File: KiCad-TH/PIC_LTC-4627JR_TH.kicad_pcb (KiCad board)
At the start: 2 copper layers, 0 parts

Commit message: PCB Routing Round 5 Begins
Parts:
- added J1: Conn_01x05_Male, Pin_Headers:Pin_Header_Straight_1x05_Pitch2.54mm, F.Cu at (95.9, 113.7)
- added J2: Conn_01x04, Connectors_JST:JST_PH_B4B-PH-K_04x2.00mm_Straight, F.Cu at (104.1, 119.4)
- added L1: LTC-4627JR, LTC-4627JR:LTC-4627JR, F.Cu at (114.5, 83.8)
- added Q1: Q_NPN_EBC, TO_SOT_Packages_THT:TO-92_Inline_Narrow_Oval, F.Cu at (119.4, 95.2)
- added Q2: Q_NPN_EBC, TO_SOT_Packages_THT:TO-92_Inline_Narrow_Oval, F.Cu at (100.3, 95.2)
- added Q3: Q_NPN_EBC, TO_SOT_Packages_THT:TO-92_Inline_Narrow_Oval, F.Cu at (125.7, 95.2)
- added Q4: Q_NPN_EBC, TO_SOT_Packages_THT:TO-92_Inline_Narrow_Oval, F.Cu at (113.0, 95.2)
- added Q5: Q_NPN_EBC, TO_SOT_Packages_THT:TO-92_Inline_Narrow_Oval, F.Cu at (106.7, 95.2)
- added R1: 120, Resistors_THT:R_Axial_DIN0207_L6.3mm_D2.5mm_P10.16mm_Horizontal, F.Cu at (98.4, 99.1)
- added R10: 1k, Resistors_THT:R_Axial_DIN0207_L6.3mm_D2.5mm_P10.16mm_Horizontal, F.Cu at (114.3, 99.1)
- added R11: 1k, Resistors_THT:R_Axial_DIN0207_L6.3mm_D2.5mm_P10.16mm_Horizontal, F.Cu at (130.2, 99.1)
- added R12: 1k, Resistors_THT:R_Axial_DIN0207_L6.3mm_D2.5mm_P10.16mm_Horizontal, F.Cu at (104.8, 99.1)
- added R13: 1k, Resistors_THT:R_Axial_DIN0207_L6.3mm_D2.5mm_P10.16mm_Horizontal, F.Cu at (123.8, 99.1)
- added R2: 120, Resistors_THT:R_Axial_DIN0207_L6.3mm_D2.5mm_P10.16mm_Horizontal, F.Cu at (133.3, 99.1)
- added R3: 120, Resistors_THT:R_Axial_DIN0207_L6.3mm_D2.5mm_P10.16mm_Horizontal, F.Cu at (120.7, 99.1)
- added R4: 120, Resistors_THT:R_Axial_DIN0207_L6.3mm_D2.5mm_P10.16mm_Horizontal, F.Cu at (111.1, 99.1)
- added R5: 120, Resistors_THT:R_Axial_DIN0207_L6.3mm_D2.5mm_P10.16mm_Horizontal, F.Cu at (117.5, 99.1)
- added R6: 120, Resistors_THT:R_Axial_DIN0207_L6.3mm_D2.5mm_P10.16mm_Horizontal, F.Cu at (95.2, 99.1)
- added R7: 120, Resistors_THT:R_Axial_DIN0207_L6.3mm_D2.5mm_P10.16mm_Horizontal, F.Cu at (101.6, 99.1)
- added R8: 120, Resistors_THT:R_Axial_DIN0207_L6.3mm_D2.5mm_P10.16mm_Horizontal, F.Cu at (127.0, 99.1)
- added R9: 1k, Resistors_THT:R_Axial_DIN0207_L6.3mm_D2.5mm_P10.16mm_Horizontal, F.Cu at (108.0, 99.1)
- added U1: PIC16F18344-P, Housings_DIP:DIP-20_W7.62mm, F.Cu at (109.9, 121.3)

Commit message: PCB #5 Looking Good Still Needs Polish
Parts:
- moved R11 29.2 mm to (101.0, 99.1)
- moved Q3 27.3 mm to (98.4, 95.2)
- moved R9 25.4 mm to (133.3, 99.1)
- moved Q5 24.1 mm to (130.8, 95.2)
- moved R1 21.6 mm to (120.0, 99.1)
- moved R10 15.9 mm to (130.2, 99.1)
- moved J1 14.0 mm to (95.9, 99.7), turned to 0 degrees
- moved R7 12.1 mm to (113.7, 99.1)
- moved Q4 12.1 mm to (125.1, 95.2)
- moved R6 10.8 mm to (106.0, 99.1)
- moved R2 10.8 mm to (122.6, 99.1)
- moved R5 8.89 mm to (108.6, 99.1)
- moved R13 6.35 mm to (117.5, 99.1)
- moved Q2 4.45 mm to (104.8, 95.2)
- moved R3 4.44 mm to (125.1, 99.1)
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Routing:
- net /VPP: track 0.00 -> 40.8 mm, vias 0 -> 4
- net /DIG_2: track 0.00 -> 38.1 mm, vias 0 -> 2
- net /I2CCL: track 0.00 -> 36.5 mm, vias 0 -> 1
- net /DIG_4: track 0.00 -> 34.9 mm, vias 0 -> 2
- net Net-(L1-Pad15): track 0.00 -> 33.4 mm, vias 0 -> 3
- net /I2CDA: track 0.00 -> 32.2 mm, vias 0 -> 1
- net Net-(L1-Pad5): track 0.00 -> 30.4 mm, vias 0 -> 2
- net /ICSPCLK: track 0.00 -> 28.2 mm, vias 0 -> 2
- net /DIG_L: track 0.00 -> 24.8 mm, vias 0 -> 2
- net Net-(L1-Pad13): track 0.00 -> 24.5 mm, vias 0 -> 2
- net Net-(R5-Pad2): track 0.00 -> 24.1 mm, vias 0 -> 2
- net Net-(R7-Pad2): track 0.00 -> 24.1 mm, vias 0 -> 2
- net Net-(R6-Pad2): track 0.00 -> 24.1 mm, vias 0 -> 2
- net Net-(R4-Pad2): track 0.00 -> 24.1 mm, vias 0 -> 2
- net Net-(L1-Pad16): track 0.00 -> 22.7 mm
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- added copper zone on F.Cu, net GND
- added copper zone on B.Cu, net VCC
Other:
- net class Default: trace_width 0.1524 -> 0.25

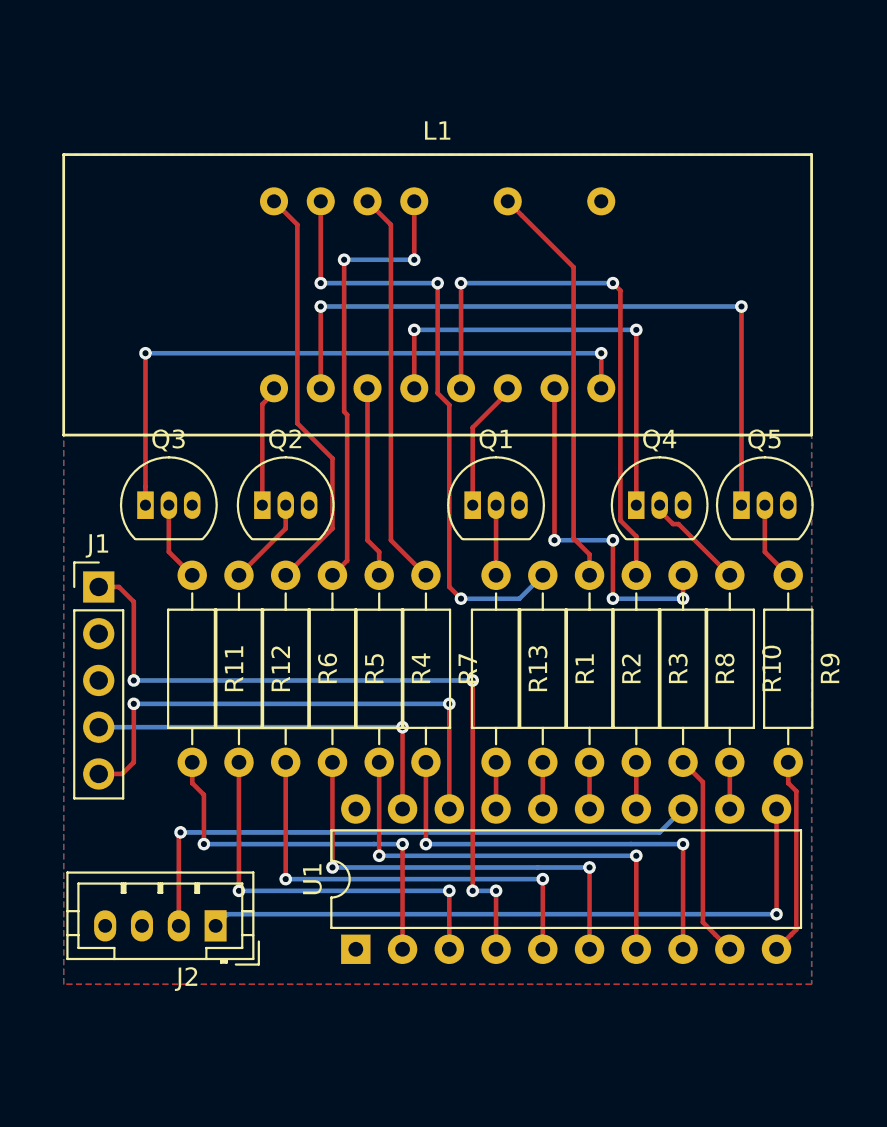
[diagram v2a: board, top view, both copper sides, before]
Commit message: PCB#5 now with Vpp pull-up resistor
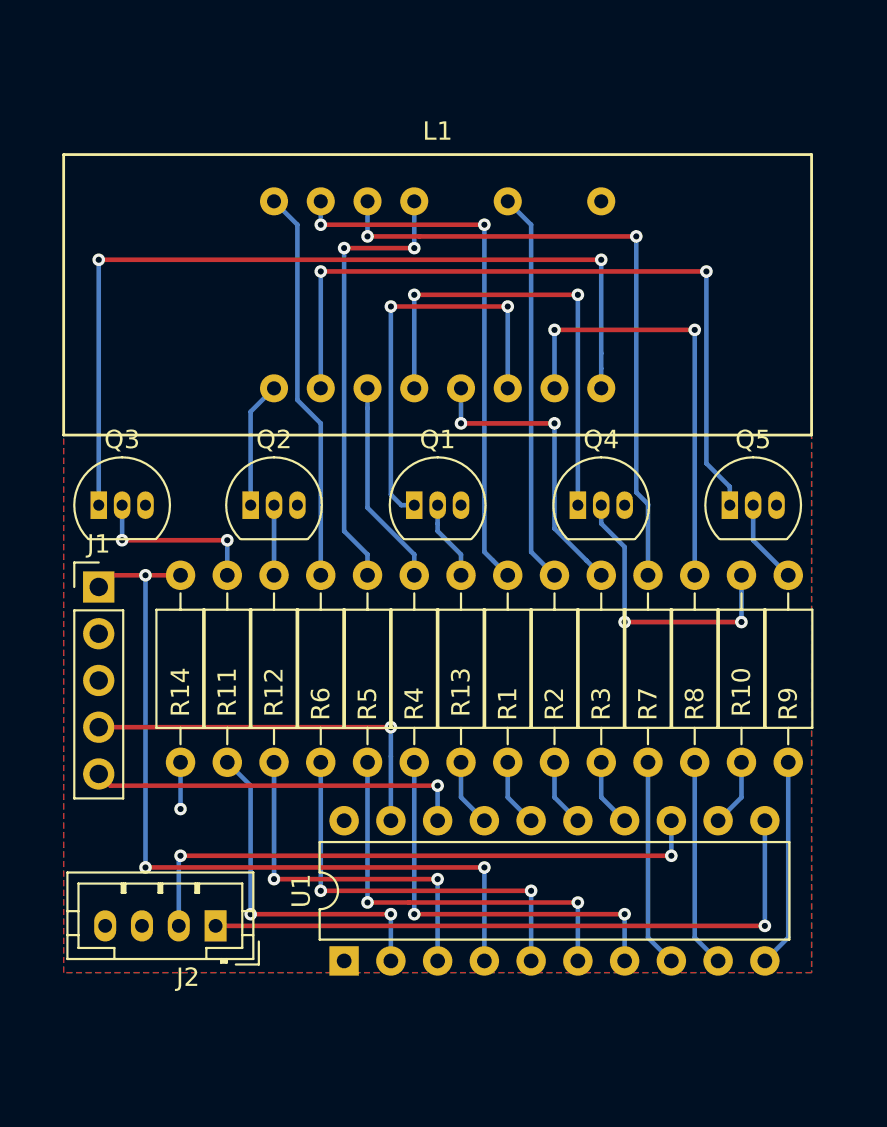
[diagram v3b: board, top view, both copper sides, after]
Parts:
- added R14: 10k, Resistors_THT:R_Axial_DIN0207_L6.3mm_D2.5mm_P10.16mm_Horizontal, F.Cu at (100.3, 99.1)
- moved R7 12.1 mm to (125.7, 99.1)
- moved Q1 3.17 mm to (113.0, 95.2)
- moved Q4 3.17 mm to (121.9, 95.2)
- moved Q3 2.54 mm to (95.9, 95.2)
- moved R1 1.91 mm to (118.1, 99.1)
- moved R11 1.91 mm to (102.9, 99.1)
- moved R12 1.91 mm to (105.4, 99.1)
- moved R13 1.91 mm to (115.6, 99.1)
- moved R2 1.91 mm to (120.7, 99.1)
- moved R3 1.91 mm to (123.2, 99.1)
- moved R4 1.91 mm to (113.0, 99.1)
- moved R5 1.91 mm to (110.5, 99.1)
- moved R6 1.91 mm to (108.0, 99.1)
- moved U1 0.90 mm to (109.2, 120.0)
- moved Q2 0.64 mm to (104.1, 95.2)
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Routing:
- net /DIG_3: track 7.23 -> 22.5 mm, vias 0 -> 2
- net Net-(L1-Pad5): track 30.4 -> 16.3 mm
- net Net-(L1-Pad14): track 21.6 -> 35.2 mm, vias 0 -> 2
- net Net-(R7-Pad2): track 24.1 -> 11.3 mm, vias 2 -> 0
- net /DIG_4: track 34.9 -> 47.6 mm
- net Net-(Q4-Pad2): track 5.56 -> 15.8 mm, vias 0 -> 2
- net /ICSPCLK: track 28.2 -> 20.6 mm, vias 2 -> 1
- net Net-(Q3-Pad2): track 4.34 -> 9.53 mm, vias 0 -> 2
- net Net-(L1-Pad7): track 19.7 -> 24.1 mm, vias 4 -> 2
- net Net-(L1-Pad15): track 33.4 -> 29.7 mm, vias 3 -> 2
- net /VPP: track 40.8 -> 44.1 mm, vias 4 -> 3
- net VCC: track 0.00 -> 2.54 mm, vias 0 -> 1
- net /DIG_2: track 38.1 -> 40.5 mm
- net Net-(R11-Pad2): track 21.2 -> 18.9 mm
- net Net-(R6-Pad2): track 24.1 -> 22.2 mm
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- added copper zone on B.Cu, net GND
- added copper zone on F.Cu, net VCC
- removed copper zone on F.Cu, net GND
- removed copper zone on B.Cu, net VCC

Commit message: Front SilkS
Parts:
- Q1 DIG_3: renamed from Q1
- Q2 DIG_1: renamed from Q2
- Q3 DIG_4: renamed from Q3
- Q4 DIG_L: renamed from Q4
- Q5 DIG_2: renamed from Q5
- R1  120: renamed from R1
- R10  1k: renamed from R10
- R11  1k: renamed from R11
- R12  1k: renamed from R12
- R13  1k: renamed from R13
- R14 10k: renamed from R14
- R2  120: renamed from R2
- R3  120: renamed from R3
- R4  120: renamed from R4
- R5  120: renamed from R5
- R6  120: renamed from R6
- R7  120: renamed from R7
- R8  120: renamed from R8
- R9   1k: renamed from R9
- renumbered J1 to ICSP, L1 to LTC-4627JR, U1 to PIC16F18345, J2 to PWR+I2C
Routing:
- net VCC: track 2.54 -> 6.35 mm, vias 1 -> 2
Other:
- board text added: ">"

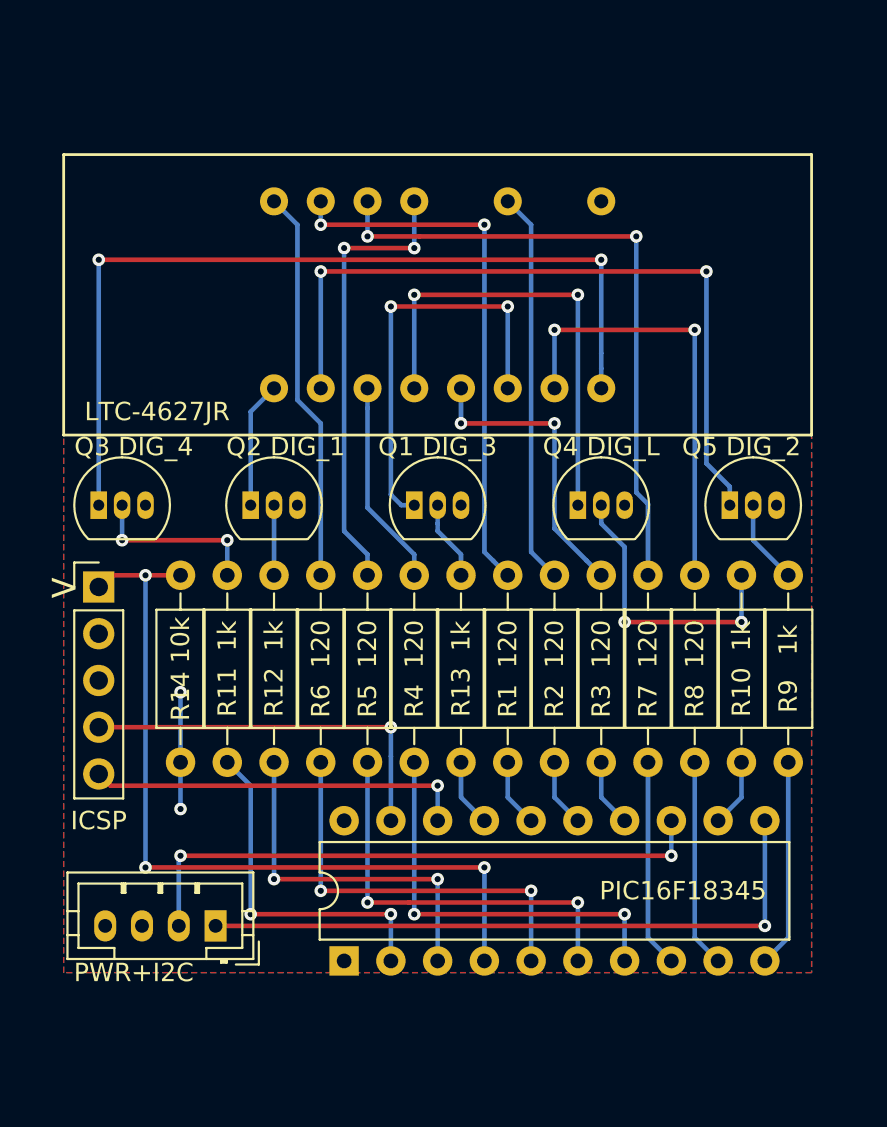
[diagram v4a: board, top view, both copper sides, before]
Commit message: Edge cut, M3 mounting holes, Back SilkS
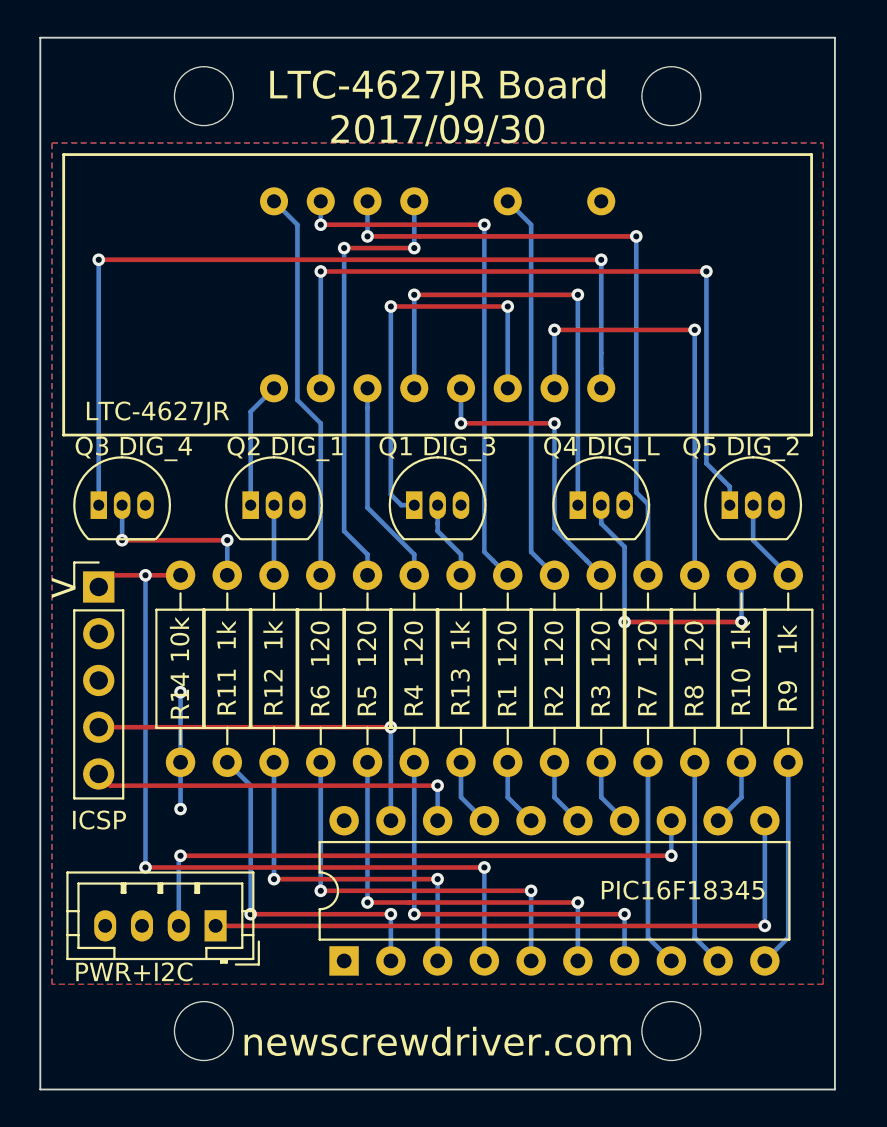
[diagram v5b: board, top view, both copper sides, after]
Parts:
- added H1: MountingHole_3.2mm_M3, Mounting_Holes:MountingHole_3.2mm_M3, F.Cu at (101.6, 73.0)
- added H2: MountingHole_3.2mm_M3, Mounting_Holes:MountingHole_3.2mm_M3, F.Cu at (127.0, 73.0)
- added H3: MountingHole_3.2mm_M3, Mounting_Holes:MountingHole_3.2mm_M3, F.Cu at (127.0, 123.8)
- added H4: MountingHole_3.2mm_M3, Mounting_Holes:MountingHole_3.2mm_M3, F.Cu at (101.6, 123.8)
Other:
- board outline added: 43.2 x 57.2 mm
- board text added: "<"
- board text added: "CD-+"
- board text added: "LTC-4627JR Board 2017/09/30"
- board text added: "newscrewdriver.com"
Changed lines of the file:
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@@
   (general
     (thickness 1.6)
-    (drawings 1)
+    (drawings 11)
     (tracks 164)
     (zones 0)
-    (modules 23)
+    (modules 27)
     (nets 39)
   )
@@
       (net 20 /DIG_1))
   )
+  (module Mounting_Holes:MountingHole_3.2mm_M3 (layer F.Cu)
+    (at 127 123.825)
+    (descr "Mounting Hole 3.2mm, no annular, M3")
+    (tags "mounting hole 3.2mm no annular m3")
+    (attr virtual)
+    (fp_text reference H3 (at 0 -4.2) (layer F.SilkS) hide
+      (effects (font (size 1 1) (thickness 0.15)))
+    )
+    (fp_text value MountingHole_3.2mm_M3 (at 0 4.2) (layer F.Fab)
+      (effects (font (size 1 1) (thickness 0.15)))
+    )
+    (fp_text user %R (at 0.3 0) (layer F.Fab)
+      (effects (font (size 1 1) (thickness 0.15)))
+    )
+    (fp_circle (center 0 0) (end 3.2 0) (layer Cmts.User) (width 0.15))
+    (fp_circle (center 0 0) (end 3.45 0) (layer F.CrtYd) (width 0.05))
+    (pad 1 np_thru_hole circle (at 0 0) (size 3.2 3.2) (drill 3.2) (layers *.Cu *.Mask))
+  )
+  (module Mounting_Holes:MountingHole_3.2mm_M3 (layer F.Cu)
+    (at 127 73.025)
+    (descr "Mounting Hole 3.2mm, no annular, M3")
+    (tags "mounting hole 3.2mm no annular m3")
+    (attr virtual)
+    (fp_text reference H2 (at 0 -4.2) (layer F.SilkS) hide
+      (effects (font (size 1 1) (thickness 0.15)))
+    )
+    (fp_text value MountingHole_3.2mm_M3 (at 0 4.2) (layer F.Fab)
+      (effects (font (size 1 1) (thickness 0.15)))
+    )
+    (fp_circle (center 0 0) (end 3.45 0) (layer F.CrtYd) (width 0.05))
+    (fp_circle (center 0 0) (end 3.2 0) (layer Cmts.User) (width 0.15))
+    (fp_text user %R (at 0.3 0) (layer F.Fab)
+      (effects (font (size 1 1) (thickness 0.15)))
+    )
+    (pad 1 np_thru_hole circle (at 0 0) (size 3.2 3.2) (drill 3.2) (layers *.Cu *.Mask))
+  )
+  (module Mounting_Holes:MountingHole_3.2mm_M3 (layer F.Cu)
+    (at 101.6 123.825)
+    (descr "Mounting Hole 3.2mm, no annular, M3")
+    (tags "mounting hole 3.2mm no annular m3")
+    (attr virtual)
+    (fp_text reference H4 (at 0 -4.2) (layer F.SilkS) hide
+      (effects (font (size 1 1) (thickness 0.15)))
+    )
+    (fp_text value MountingHole_3.2mm_M3 (at 0 4.2) (layer F.Fab)
+      (effects (font (size 1 1) (thickness 0.15)))
+    )
+    (fp_circle (center 0 0) (end 3.45 0) (layer F.CrtYd) (width 0.05))
+    (fp_circle (center 0 0) (end 3.2 0) (layer Cmts.User) (width 0.15))
+    (fp_text user %R (at 0.3 0) (layer F.Fab)
+      (effects (font (size 1 1) (thickness 0.15)))
+    )
+    (pad 1 np_thru_hole circle (at 0 0) (size 3.2 3.2) (drill 3.2) (layers *.Cu *.Mask))
+  )
+  (module Mounting_Holes:MountingHole_3.2mm_M3 (layer F.Cu)
+    (at 101.6 73.025)
+    (descr "Mounting Hole 3.2mm, no annular, M3")
+    (tags "mounting hole 3.2mm no annular m3")
+    (attr virtual)
+    (fp_text reference H1 (at 0 -4.2) (layer F.SilkS) hide
+      (effects (font (size 1 1) (thickness 0.15)))
+    )
+    (fp_text value MountingHole_3.2mm_M3 (at 0 4.2) (layer F.Fab)
+      (effects (font (size 1 1) (thickness 0.15)))
+    )
+    (fp_text user %R (at 0.3 0) (layer F.Fab)
+      (effects (font (size 1 1) (thickness 0.15)))
+    )
+    (fp_circle (center 0 0) (end 3.2 0) (layer Cmts.User) (width 0.15))
+    (fp_circle (center 0 0) (end 3.45 0) (layer F.CrtYd) (width 0.05))
+    (pad 1 np_thru_hole circle (at 0 0) (size 3.2 3.2) (drill 3.2) (layers *.Cu *.Mask))
+  )
   (module Pin_Headers:Pin_Header_Straight_1x05_Pitch2.54mm (layer F.Cu)
     (at 95.885 99.695)
@@
       (rotate (xyz 0 0 0))
     )
+  )
+  (gr_text CD-+ (at 99.06 120.65) (layer B.SilkS)
+    (effects (font (size 1.5 1.5) (thickness 0.3)) (justify mirror))
+  )
+  (gr_text < (at 93.98 99.695) (layer B.SilkS)
+    (effects (font (size 1.5 1.5) (thickness 0.3)) (justify mirror))
+  )
+  (gr_text newscrewdriver.com (at 114.3 104.14) (layer B.SilkS)
+    (effects (font (size 1.5 1.5) (thickness 0.3)) (justify mirror))
+  )
+  (gr_text "LTC-4627JR Board\n2017/09/30" (at 114.3 73.66) (layer B.SilkS)
+    (effects (font (size 1.5 1.5) (thickness 0.3)) (justify mirror))
+  )
+  (gr_line (start 92.71 127) (end 92.71 69.85) (layer Edge.Cuts) (width 0.1))
+  (gr_line (start 135.89 127) (end 92.71 127) (layer Edge.Cuts) (width 0.1))
+  (gr_line (start 135.89 69.85) (end 135.89 127) (layer Edge.Cuts) (width 0.1))
+  (gr_line (start 92.71 69.85) (end 135.89 69.85) (layer Edge.Cuts) (width 0.1))
+  (gr_text newscrewdriver.com (at 114.3 124.46) (layer F.SilkS)
+    (effects (font (size 1.5 1.5) (thickness 0.3)))
+  )
+  (gr_text "LTC-4627JR Board\n2017/09/30" (at 114.3 73.66) (layer F.SilkS)
+    (effects (font (size 1.5 1.5) (thickness 0.3)))
   )
   (gr_text > (at 93.98 99.695) (layer F.SilkS)
@@
   (segment (start 115.57 109.22) (end 115.57 111.125) (width 0.25) (layer B.Cu) (net 38))
   (segment (start 115.57 111.125) (end 116.84 112.395) (width 0.25) (layer B.Cu) (net 38))
+  (zone (net 4) (net_name VCC) (layer F.Cu) (hatch edge 0.508)
+    (connect_pads (clearance 0.508))
+    (min_thickness 0.254)
+    (fill yes (arc_segments 16) (thermal_gap 0.508) (thermal_bridge_width 0.508))
+    (polygon
+      (pts
+        (xy 93.345 75.565) (xy 135.255 75.565) (xy 135.255 121.285) (xy 93.345 121.285)
+      )
+    )
+  )
   (zone (net 3) (net_name GND) (layer B.Cu) (hatch edge 0.508)
     (connect_pads (clearance 0.508))
@@
     (polygon
       (pts
-        (xy 93.98 76.2) (xy 134.62 76.2) (xy 134.62 120.65) (xy 93.98 120.65)
+        (xy 93.345 75.565) (xy 135.255 75.565) (xy 135.255 121.285) (xy 93.345 121.285)
       )
     )
-  )
-  (zone (net 4) (net_name VCC) (layer F.Cu) (hatch edge 0.508)
-    (connect_pads (clearance 0.508))
-    (min_thickness 0.254)
-    (fill yes (arc_segments 16) (thermal_gap 0.508) (thermal_bridge_width 0.508))
-    (polygon
-      (pts
-        (xy 93.98 76.2) (xy 134.62 76.2) (xy 134.62 120.65) (xy 93.98 120.65)
-      )
-    )
